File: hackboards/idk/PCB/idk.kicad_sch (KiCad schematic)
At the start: 205 parts, among them U1 Raspberry_Pi_Pico

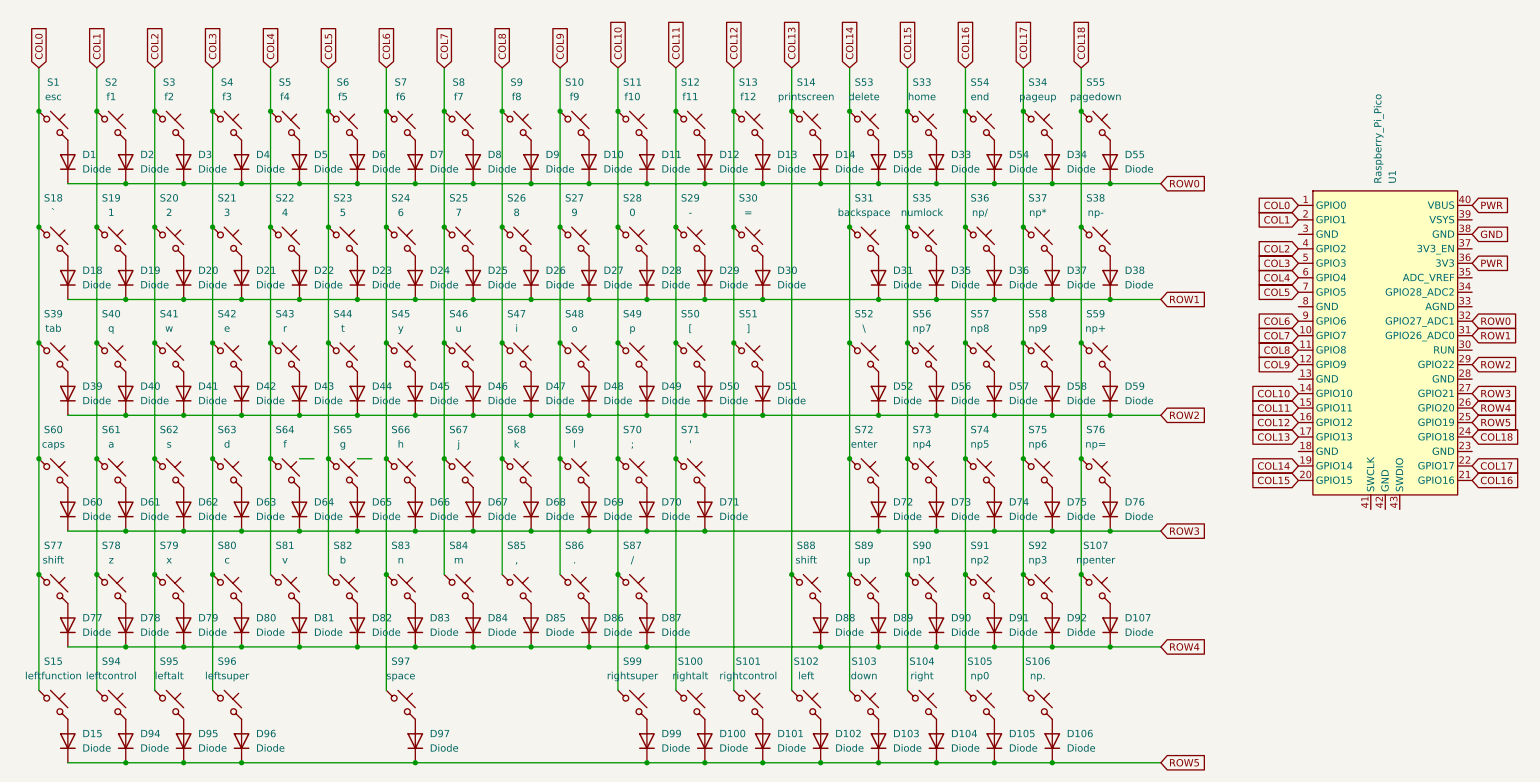
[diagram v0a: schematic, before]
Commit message: changed keyboard name
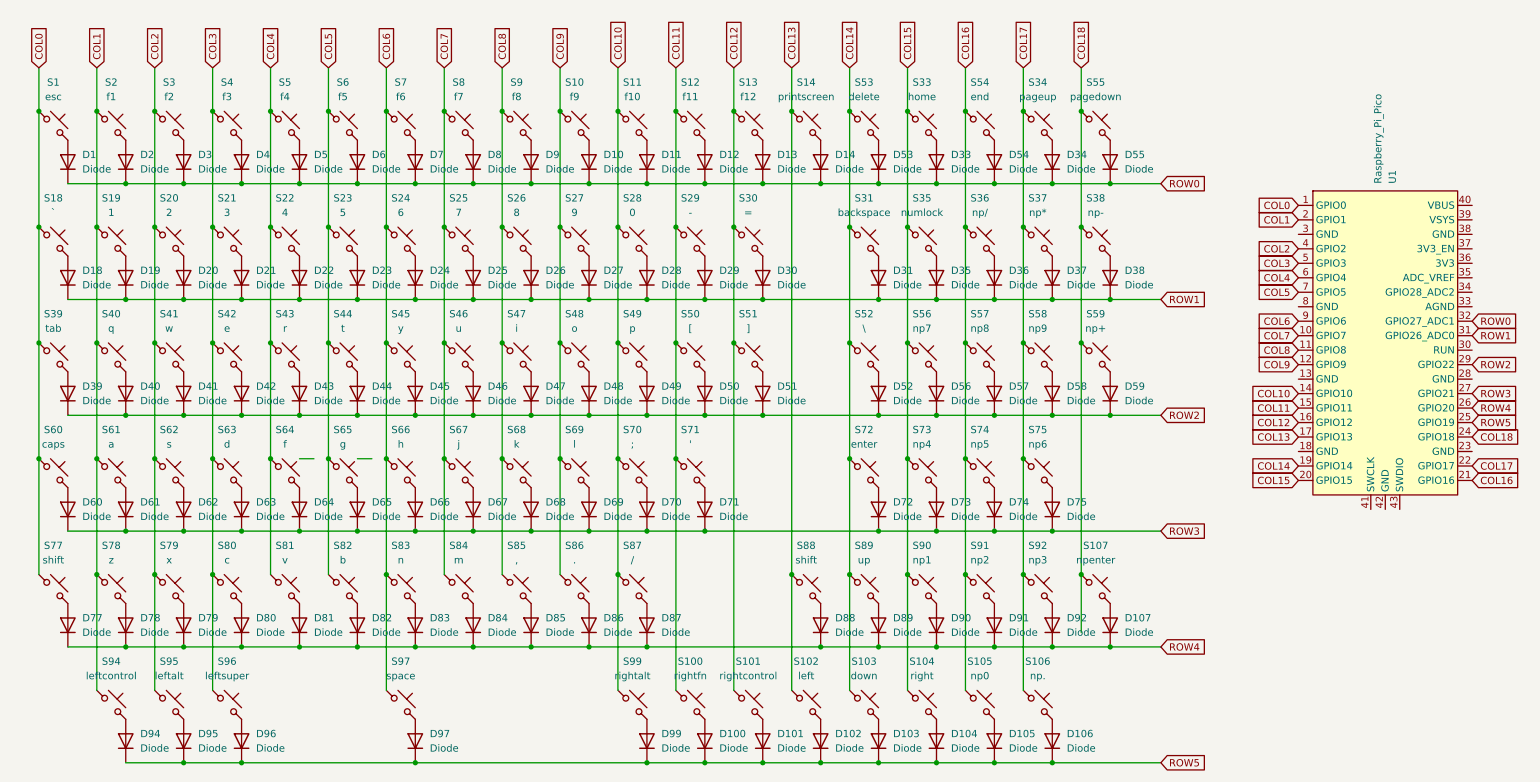
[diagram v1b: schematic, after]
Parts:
- removed D15, D76: Diode, ScottoKeebs_Components:Diode_DO-35, symbol ScottoKeebs:Placeholder_Diode
- removed S15: leftfunction, ScottoKeebs_Hotswap:Hotswap_MX_1.00u, symbol ScottoKeebs:Placeholder_Keyswitch
- removed S76: np=, ScottoKeebs_Hotswap:Hotswap_MX_1.00u, symbol ScottoKeebs:Placeholder_Keyswitch
- S1, S10, S101, S102, S103, S104, S105, S106, S11, S12, S13, S14, S18, S19, S2, S20, S21, S22, S23, S24, S25, S26, S27, S28, S29, S3, S30, S33, S34, S35, S36, S37, S38, S4, S40, S41, S42, S43, S44, S45, S46, S47, S48, S49, S5, S50, S51, S53, S54, S55, S56, S57, S58, S6, S61, S62, S63, S64, S65, S66, S67, S68, S69, S7, S70, S71, S73, S74, S75, S78, S79, S8, S80, S81, S82, S83, S84, S85, S86, S87, S89, S9, S90, S91, S92: footprint ScottoKeebs_Hotswap:Hotswap_MX_1.00u -> ScottoKeebs_MX:MX_PCB_1.00u
- S100: value rightalt -> rightfn; footprint ScottoKeebs_Hotswap:Hotswap_MX_1.00u -> ScottoKeebs_MX:MX_PCB_1.00u
- S107: footprint ScottoKeebs_Hotswap:Hotswap_MX_2.00u_90deg -> ScottoKeebs_MX:MX_PCB_2.00u_90deg
- S31: footprint ScottoKeebs_Hotswap:Hotswap_MX_2.00u -> ScottoKeebs_MX:MX_PCB_2.00u
- S39, S52: footprint ScottoKeebs_Hotswap:Hotswap_MX_1.50u -> ScottoKeebs_MX:MX_PCB_1.50u
- S59: footprint ScottoKeebs_Hotswap:Hotswap_MX_1.00u -> ScottoKeebs_MX:MX_PCB_2.00u_90deg
- S60, S88: footprint ScottoKeebs_Hotswap:Hotswap_MX_1.75u -> ScottoKeebs_MX:MX_PCB_1.75u
- S72, S77: footprint ScottoKeebs_Hotswap:Hotswap_MX_2.25u -> ScottoKeebs_MX:MX_PCB_2.25u
- S94, S95, S96: footprint ScottoKeebs_Hotswap:Hotswap_MX_1.00u -> ScottoKeebs_MX:MX_Plate_1.25u
- S97: footprint ScottoKeebs_Hotswap:Hotswap_MX_6.00u -> ScottoKeebs_MX:MX_PCB_6.25u
- S99: value rightsuper -> rightalt; footprint ScottoKeebs_Hotswap:Hotswap_MX_1.00u -> ScottoKeebs_MX:MX_PCB_1.00u
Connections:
- net GND: no longer names the net of U1.38 (GND)
- net PWR: no longer names the net of U1.36 (3V3)
- net PWR: no longer U1.40 (VBUS)
